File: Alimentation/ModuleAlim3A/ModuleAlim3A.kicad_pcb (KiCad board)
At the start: 4 copper layers, 54.8 x 40.2 mm, 18 parts, among them J1 Conn_01x05, J2 Conn_01x02, J3 OUTPUT, U1 PTN78060W_EUW-7, U2 ACS712xLCTR-20A

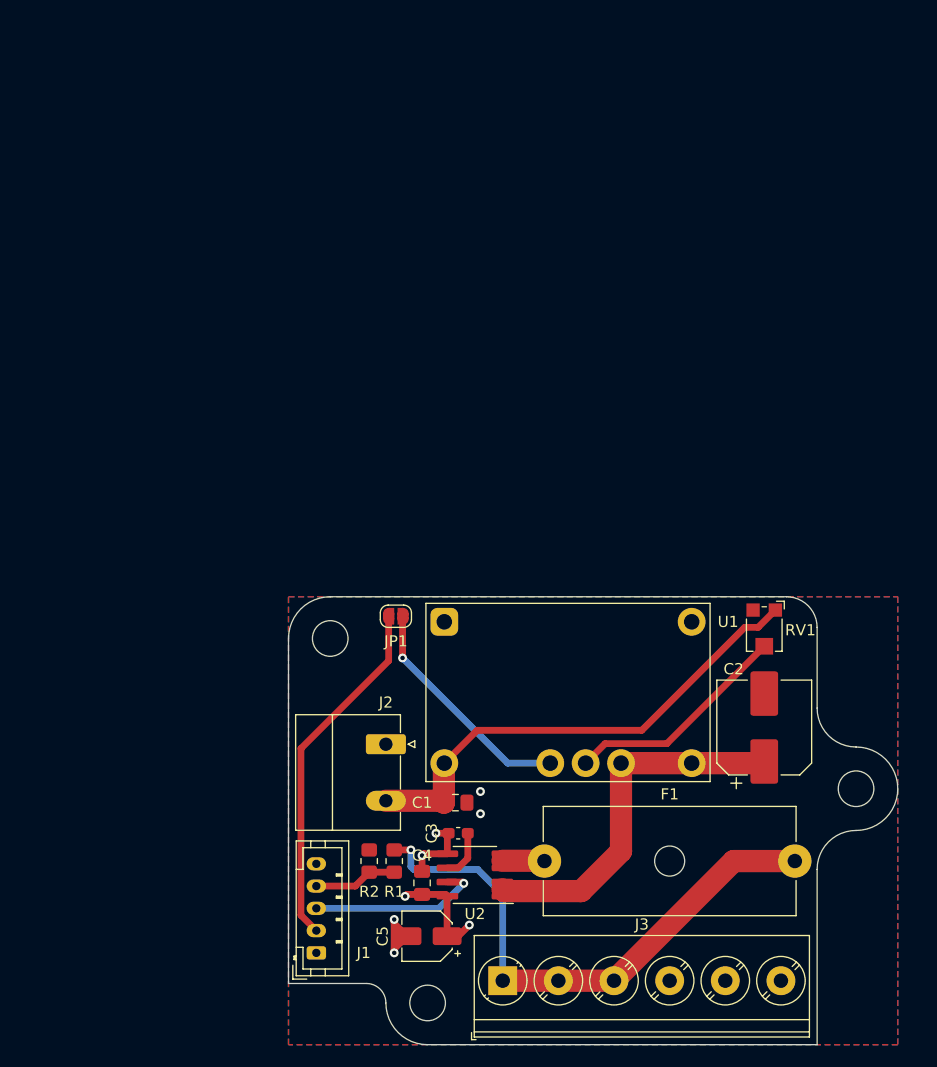
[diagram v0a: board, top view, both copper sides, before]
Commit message: Module alim ISO, clean master alim
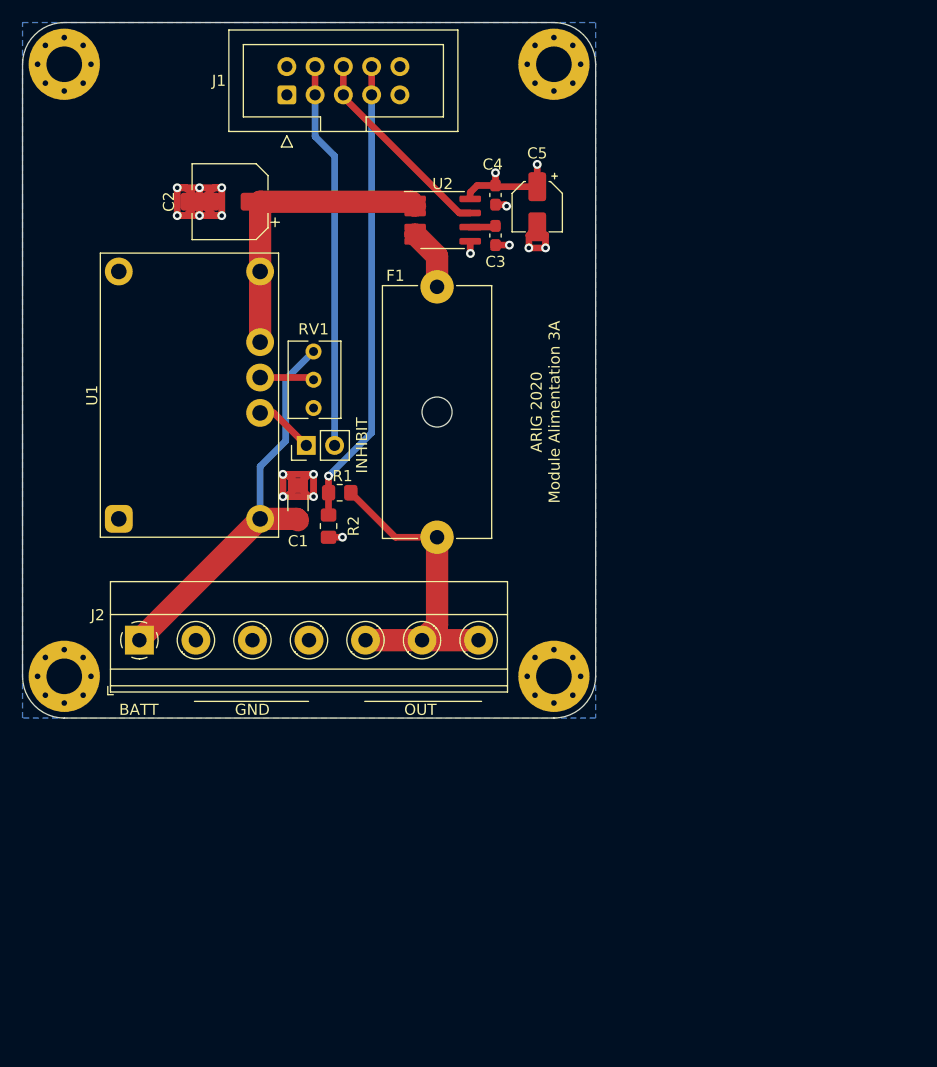
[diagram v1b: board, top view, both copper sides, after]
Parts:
- removed J3: OUTPUT, TerminalBlock_Phoenix:TerminalBlock_Phoenix_PT-1,5-6-5.0-H_1x06_P5.00mm_Horizontal
- removed JP1: /INHIBIT, Jumper:SolderJumper-2_P1.3mm_Open_RoundedPad1.0x1.5mm
- added H4: MountingHole_Pad, MountingHole:MountingHole_3.2mm_M3_Pad_Via, F.Cu at (132.6, 100.2)
- added J4: INHIBIT, Connector_PinHeader_2.54mm:PinHeader_1x02_P2.54mm_Vertical, F.Cu at (110.3, 79.4)
- C1: footprint Capacitor_SMD:C_0805_2012Metric_Pad1.18x1.45mm_HandSolder -> Capacitor_SMD:C_1206_3216Metric_Pad1.33x1.80mm_HandSolder
- C2: value 0.22m -> 100u; footprint Capacitor_SMD:CP_Elec_8x6.2 -> Capacitor_SMD:CP_Elec_6.3x7.7
- C4: footprint Capacitor_SMD:C_0805_2012Metric_Pad1.18x1.45mm_HandSolder -> Capacitor_SMD:C_0603_1608Metric_Pad1.08x0.95mm_HandSolder
- F1: value 3A -> 6A
- H1, H2, H3: value MountingHole -> MountingHole_Pad; footprint MountingHole:MountingHole_3.2mm_M3 -> MountingHole:MountingHole_3.2mm_M3_Pad_Via
- J1: value Conn_01x05 -> Cmd; footprint Connector_JST:JST_PH_B5B-PH-K_1x05_P2.00mm_Vertical -> Connector_IDC:IDC-Header_2x05_P2.54mm_Vertical
- J2: value Conn_01x02 -> POWER; footprint Connector_Phoenix_MC_HighVoltage:PhoenixContact_MC_1,5_2-G-5.08_1x02_P5.08mm_Horizontal -> TerminalBlock_Phoenix:TerminalBlock_Phoenix_MKDS-1,5-7-5.08_1x07_P5.08mm_Horizontal
- RV1: footprint Potentiometer_SMD:Potentiometer_Bourns_TC33X_Vertical -> Potentiometer_THT:Potentiometer_Bourns_3266Y_Vertical
- moved H3 96.4 mm to (88.6, 45.1)
- moved J1 77.1 mm to (108.6, 47.9)
- moved C2 67.4 mm to (103.5, 57.5), turned to 180 degrees
- moved C5 66.3 mm to (131.1, 58.0), turned to 270 degrees
- moved C4 62.2 mm to (127.3, 56.9), turned to 270 degrees
- moved U2 58.9 mm to (122.6, 59.1), turned to 0 degrees
- moved H1 55.4 mm to (132.6, 45.1)
- moved C3 53.8 mm to (127.3, 60.5), turned to 270 degrees
- moved F1 52.5 mm to (122.1, 65.2), turned to 270 degrees
- moved RV1 47.6 mm to (111.0, 71.0), turned to 90 degrees
- moved H2 43.9 mm to (88.6, 100.2)
- moved R1 33.5 mm to (113.3, 83.7), turned to 180 degrees
- moved U1 30.7 mm to (93.5, 86.0), turned to 90 degrees
- moved C1 30.4 mm to (109.6, 84.6), turned to 90 degrees
- moved R2 30.3 mm to (112.3, 86.7), turned to 270 degrees
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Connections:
- H1 pad 1: (no net) -> GND
- H2 pad 1: (no net) -> GND
- H3 pad 1: (no net) -> GND
- J1 pad 2: /EN -> +5V
- J1 pad 3: /ANA_CURRENT -> /EN
- J1 pad 4: /ANA_VOLT -> /EN
- J1 pad 5: GND -> /ANA_CURRENT
- J2 pad 1: GND -> +BATT
- J2 pad 2: +BATT -> GND
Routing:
- net GND: track 13.7 -> 52.9 mm, vias 6 -> 16
- net /ANA_VOLT: track 7.52 -> 41.9 mm, vias 0 -> 1
- net /OUT: track 50.7 -> 29.4 mm, vias 1 -> 0
- net Net-(J4-Pad1): track 21.0 -> 5.36 mm, vias 1 -> 0
- net Net-(RV1-Pad2): track 20.4 -> 4.88 mm
- net +BATT: track 44.3 -> 35.9 mm
- net /VO: track 34.3 -> 28.0 mm
- net /ANA_CURRENT: track 15.7 -> 18.4 mm, vias 1 -> 0
- net /EN: track 32.1 -> 34.8 mm
- net Net-(C3-Pad1): track 4.45 -> 2.32 mm
- net Net-(F1-Pad1): track 5.06 -> 6.81 mm
- removed copper zone on F.Cu, net GND
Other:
- board size 54.8 x 40.2 mm -> 51.5 x 62.5 mm
- board text added: "ARIG 2020 Module Alimentation 3A"
- board text added: "BATT"
- board text added: "GND"
- board text added: "OUT"

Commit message: Modules Alim 3A et 6A uniforme sans mesure courant/tension
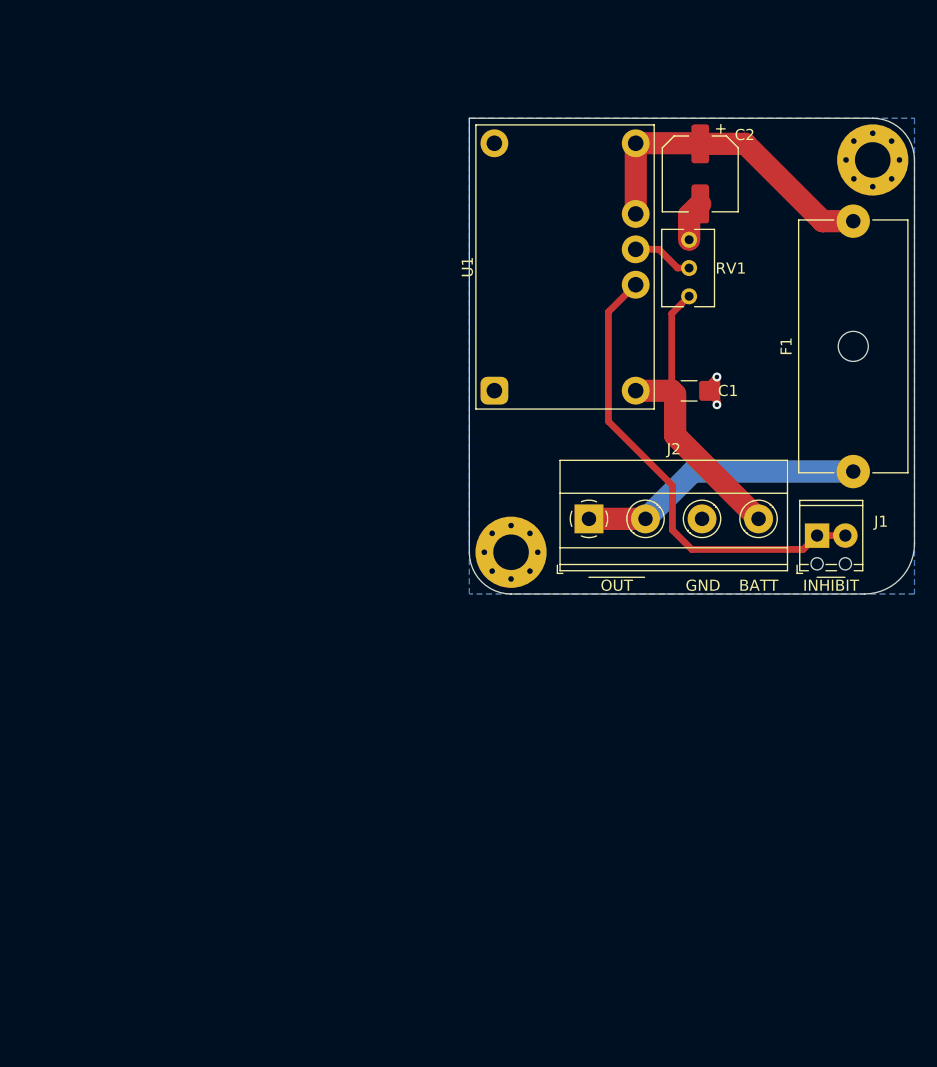
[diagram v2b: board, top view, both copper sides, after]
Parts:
- removed C3: 1n, Capacitor_SMD:C_0603_1608Metric_Pad1.08x0.95mm_HandSolder
- removed C4: 100n, Capacitor_SMD:C_0603_1608Metric_Pad1.08x0.95mm_HandSolder
- removed C5: 1u, Capacitor_SMD:CP_Elec_4x5.3
- removed H3, H4: MountingHole_Pad, MountingHole:MountingHole_3.2mm_M3_Pad_Via
- removed J4: INHIBIT, Connector_PinHeader_2.54mm:PinHeader_1x02_P2.54mm_Vertical
- removed R1: 10K, Resistor_SMD:R_0805_2012Metric_Pad1.20x1.40mm_HandSolder
- removed R2: 6.2K, Resistor_SMD:R_0805_2012Metric_Pad1.20x1.40mm_HandSolder
- removed U2: ACS712xLCTR-20A, Package_SO:SOIC-8_3.9x4.9mm_P1.27mm
- J1: value Cmd -> Inhibit; footprint Connector_IDC:IDC-Header_2x05_P2.54mm_Vertical -> TerminalBlock_Phoenix:TerminalBlock_Phoenix_MPT-0,5-2-2.54_1x02_P2.54mm_Horizontal
- J2: value POWER -> Alim. IN / OUT; footprint TerminalBlock_Phoenix:TerminalBlock_Phoenix_MKDS-1,5-7-5.08_1x07_P5.08mm_Horizontal -> TerminalBlock_Phoenix:TerminalBlock_Phoenix_MKDS-1,5-4-5.08_1x04_P5.08mm_Horizontal
- moved H2 86.2 mm to (161.2, 53.8)
- moved J1 62.0 mm to (156.2, 87.5), turned to 0 degrees
- moved H1 44.0 mm to (128.8, 89.0)
- moved C2 42.3 mm to (145.8, 55.0), turned to 270 degrees
- moved J2 41.8 mm to (135.8, 86.0)
- moved F1 40.9 mm to (159.5, 81.8), turned to 90 degrees
- moved C1 36.6 mm to (144.8, 74.5), turned to 0 degrees
- moved U1 35.7 mm to (127.2, 74.5)
- moved RV1 34.1 mm to (144.8, 66.0), turned to 270 degrees
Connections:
- C2 pad 1: /VO -> Net-(C2-Pad1)
- F1 pad 1: Net-(F1-Pad1) -> /OUT
- F1 pad 2: /OUT -> Net-(C2-Pad1)
- J1 pad 1: +5V -> /EN
- J1 pad 2: +5V -> /EN
- J2 pad 1: +BATT -> /OUT
- J2 pad 2: GND -> /OUT
- J2 pad 4: GND -> +BATT
- U1 pad 3: Net-(J4-Pad1) -> /EN
- U1 pad 5: /VO -> Net-(C2-Pad1)
- U1 pad 6: /VO -> Net-(C2-Pad1)
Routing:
- net GND: track 52.9 -> 9.41 mm, vias 16 -> 2
- net /ANA_VOLT: track 41.9 -> 0.00 mm, vias 1 -> 0
- net Net-(C2-Pad1): track 0.00 -> 28.8 mm
- net /VO: track 28.0 -> 0.00 mm
- net /ANA_CURRENT: track 18.4 -> 0.00 mm
- net +5V: track 10.0 -> 0.00 mm, vias 2 -> 0
- net +BATT: track 35.9 -> 27.1 mm
- net /EN: track 34.8 -> 42.2 mm
- net Net-(F1-Pad1): track 6.81 -> 0.00 mm
- net Net-(J4-Pad1): track 5.36 -> 0.00 mm
- net /OUT: track 29.4 -> 25.5 mm
- net Net-(C3-Pad1): track 2.32 -> 0.00 mm
- net Net-(RV1-Pad2): track 4.88 -> 5.50 mm
- removed copper zone on In2.Cu, net +5V
- removed copper zone on In1.Cu, net GND
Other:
- board size 51.5 x 62.5 mm -> 40 x 42.8 mm
- copper layers 4 -> 2
- board text added: "INHIBIT"
- board text removed: "ARIG 2020 Module Alimentation 3A"

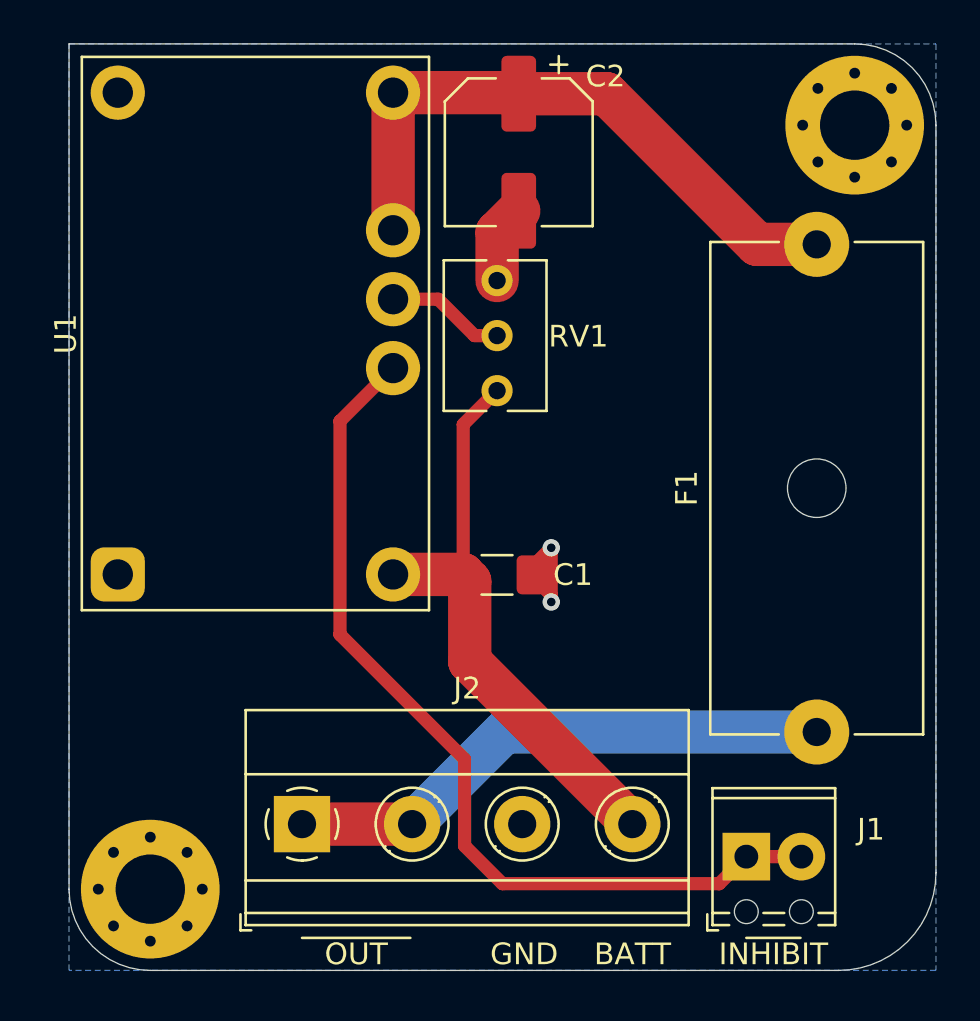
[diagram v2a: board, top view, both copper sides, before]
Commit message: Finalisation modules 3A et 6A, routage master alim
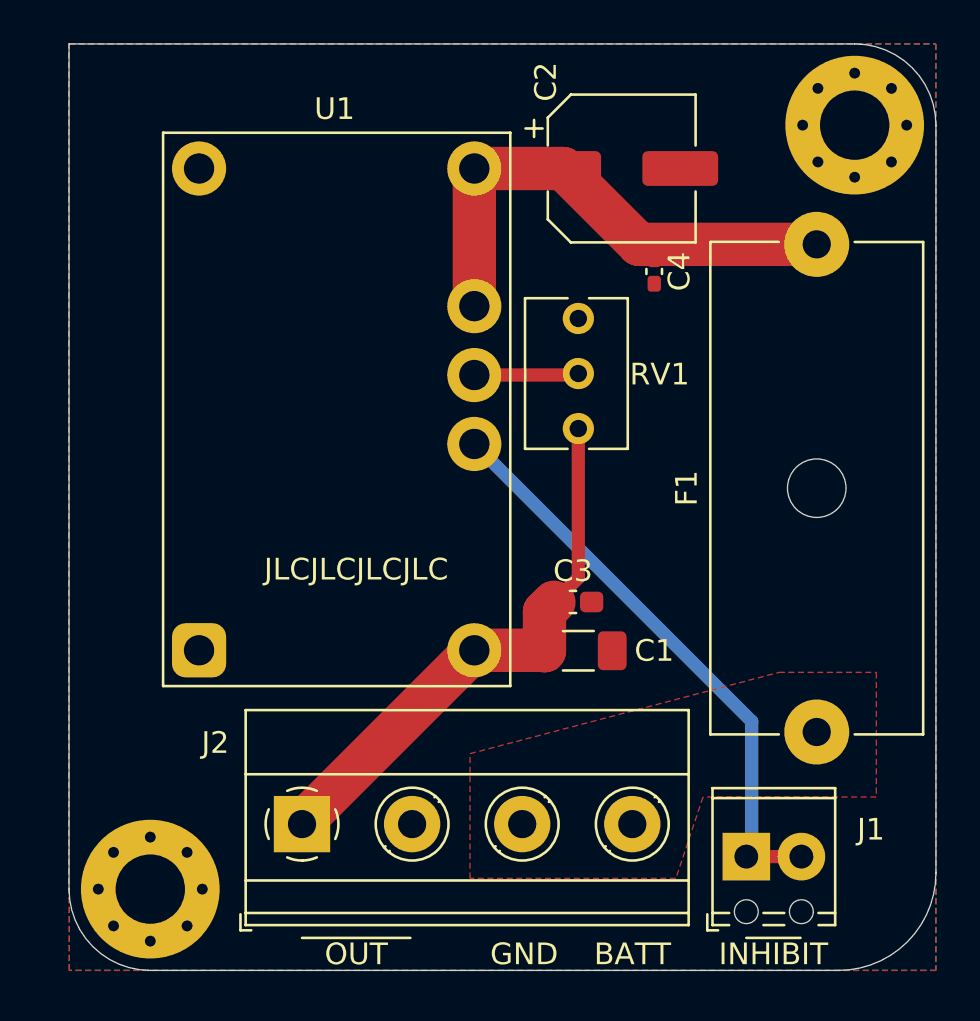
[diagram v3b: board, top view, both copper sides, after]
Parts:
- added C3: 1u, Capacitor_SMD:C_0603_1608Metric_Pad1.08x0.95mm_HandSolder, F.Cu at (148.2, 75.8)
- added C4: 1u, Capacitor_SMD:C_0402_1005Metric_Pad0.74x0.62mm_HandSolder, F.Cu at (152.0, 60.5)
- added G***: LOGO, ARIG:Logo_ARIG_12_6x6_6, B.Cu at (136.0, 64.8)
- moved C1 5.13 mm to (148.5, 78.0)
- moved U1 5.13 mm to (131.0, 78.0)
- moved C2 4.81 mm to (150.5, 55.8), turned to 0 degrees
- moved RV1 4.14 mm to (148.5, 67.8)
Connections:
- J2 pad 1: /OUT -> +BATT
- J2 pad 2: /OUT -> GND
- J2 pad 3: GND -> /OUT
- J2 pad 4: +BATT -> /OUT
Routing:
- net /OUT: track 25.5 -> 0.00 mm
- net /EN: track 42.2 -> 27.0 mm
- net GND: track 9.41 -> 0.00 mm, vias 2 -> 0
- net Net-(C2-Pad1): track 28.8 -> 23.6 mm
- net +BATT: track 27.1 -> 25.4 mm
- net Net-(RV1-Pad2): track 5.50 -> 4.83 mm
- added copper zone on F.Cu, net /OUT
- added copper zone on F.Cu, net GND
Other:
- board text added: "Alimentation Module 3A 2020"
- board text added: "JLCJLCJLCJLC"

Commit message: Rework suite point robot
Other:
- outline, holes or cut-outs redrawn

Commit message: Finalisation alimentations
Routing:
- net /OUT: track 0.00 -> 15.4 mm
- removed copper zone on F.Cu, net /OUT

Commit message: Finalisation pour commande pack Alimentation 14/02/2021
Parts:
- C3: footprint Capacitor_SMD:C_0603_1608Metric_Pad1.08x0.95mm_HandSolder -> Capacitor_SMD:C_0805_2012Metric_Pad1.18x1.45mm_HandSolder
- moved C3 0.25 mm to (148.0, 75.8)

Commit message: Potar THT module 3A
# Liste des mots clés de titre de commit (version courte -> résultat long)
# r <num> -> Récupération du Redmine (Redmine #<num> : <titre_du_redmine>)
# t <titre> -> Technique : <titre>
# f <titre> -> Fix : <titre>
# ty <titre> -> Typo : <titre>
# d <titre> -> Doc : <titre>
# s <titre> -> Sécurité : <titre>
# u <titre> -> UI : <titre>
# c <titre> -> CI : <titre>
# WIP <desc>
# [skip ci] en début de titre de commit permet de ne pas déclencher de build
#
# Chaque ligne de description ajouté sera préfixé automatiquement d'une puce.
#
# Pour la saisie de temps automatique lors de l'écriture d'un commit le format est le suivant :
# /spend <options>
#
# NB : Plusieurs /spend peuvent être défini sur un même commit
#
# Les options sont :
# - Temps en heure (ie 0.25). Obligatoire
# - Numéro de redmine. Facultatif si le commit porte sur un redmine avec la syntaxe courte ou longue.
# - Catégorie de l'imputation. Facultatif. Récupération par les premières lettres en format court, si non défini Développement sera utilisé
# - Date de l'imputation au format ISO8601 (ie 2021-02-23)
#
# NB : L'imputation n'est pas bloquante pour le message de commit si une erreur survient.
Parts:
- RV1: footprint Potentiometer_THT:Potentiometer_Bourns_3266Y_Vertical -> Potentiometer_THT:Potentiometer_Bourns_3296W_Vertical
